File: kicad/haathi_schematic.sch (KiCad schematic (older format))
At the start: 0 parts

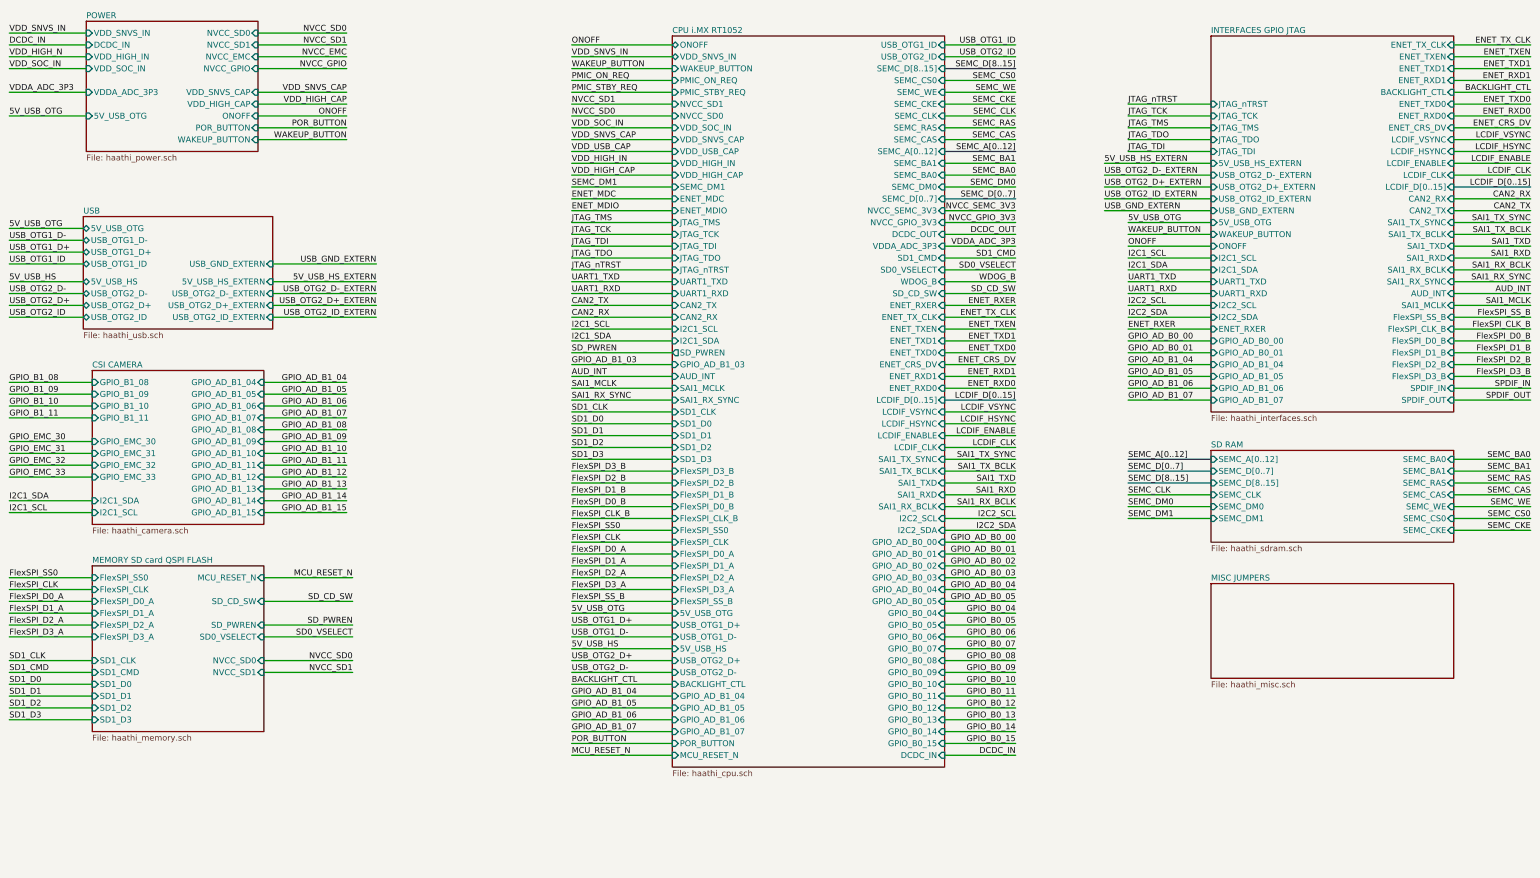
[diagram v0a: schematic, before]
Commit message: Rearrange buttons and LED pin connections
LED pins go to PWM pins
Switches go to previously SPDIF_IN and OUT pins
FlexSPI 2 pins freed up

Signed-off-by: Kumar Abhishek <abhishek@theembeddedkitchen.net>
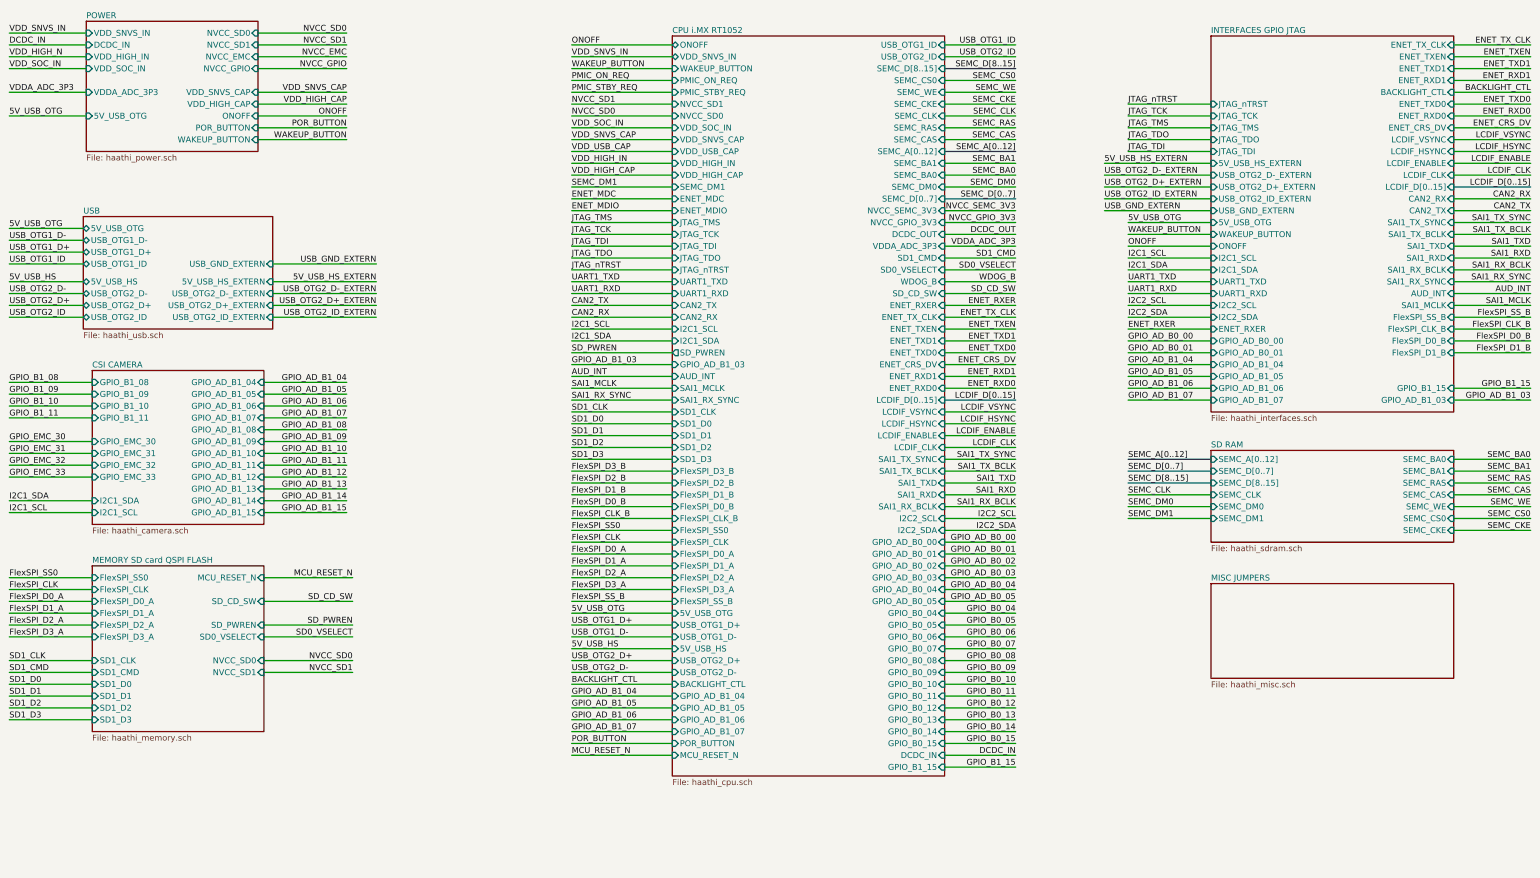
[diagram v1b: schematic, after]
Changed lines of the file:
@@
 EESchema Schematic File Version 4
-LIBS:haathi_schematic-cache
+LIBS:haathi-cache
 EELAYER 26 0
 EELAYER END
 $Descr A3 16535 11693
 encoding utf-8
-Sheet 1 9
+Sheet 3 11
 Title "haathi_cam"
 Date "2018-03-11"
@@
 $EndSheet
 $Sheet
-S 7950 1575 2300 6175
+S 7950 1575 2300 6250
 U 5A6307C3
 F0 "CPU i.MX RT1052" 50
@@
 F122 "USB_OTG1_ID" I R 10250 1650 50
 F123 "USB_OTG2_ID" I R 10250 1750 50
+F124 "GPIO_B1_15" I R 10250 7750 50
 $EndSheet
 $Sheet
@@
 F53 "GPIO_AD_B1_06" I L 12500 4550 50
 F54 "GPIO_AD_B1_07" I L 12500 4650 50
-F55 "FlexSPI_D2_B" I R 14550 4350 50
-F56 "FlexSPI_D3_B" I R 14550 4450 50
-F57 "SPDIF_IN" I R 14550 4550 50
-F58 "SPDIF_OUT" I R 14550 4650 50
+F55 "GPIO_B1_15" I R 14550 4550 50
+F57 "GPIO_AD_B1_03" I R 14550 4650 50
 $EndSheet
 $Sheet
@@
 Wire Wire Line
 	14550 4250 15200 4250
-Wire Wire Line
-	14550 4350 15200 4350
-Wire Wire Line
-	14550 4450 15200 4450
-Wire Wire Line
-	14550 4550 15200 4550
 Wire Wire Line
 	14550 4650 15200 4650
@@
 Text Label 15200 4250 2    50   ~ 0
 FlexSPI_D1_B
-Text Label 15200 4350 2    50   ~ 0
-FlexSPI_D2_B
-Text Label 15200 4450 2    50   ~ 0
-FlexSPI_D3_B
-Text Label 15200 4550 2    50   ~ 0
-SPDIF_IN
 Text Label 15200 4650 2    50   ~ 0
-SPDIF_OUT
+GPIO_AD_B1_03
 Wire Bus Line
 	12500 5150 11800 5150
@@
 Text Label 10850 1750 2    50   ~ 0
 USB_OTG2_ID
+Text Label 15200 4550 2    50   ~ 0
+GPIO_B1_15
+Wire Wire Line
+	10250 7750 10850 7750
+Text Label 10850 7750 2    50   ~ 0
+GPIO_B1_15
+Wire Wire Line
+	14550 4550 15200 4550
 $EndSCHEMATC

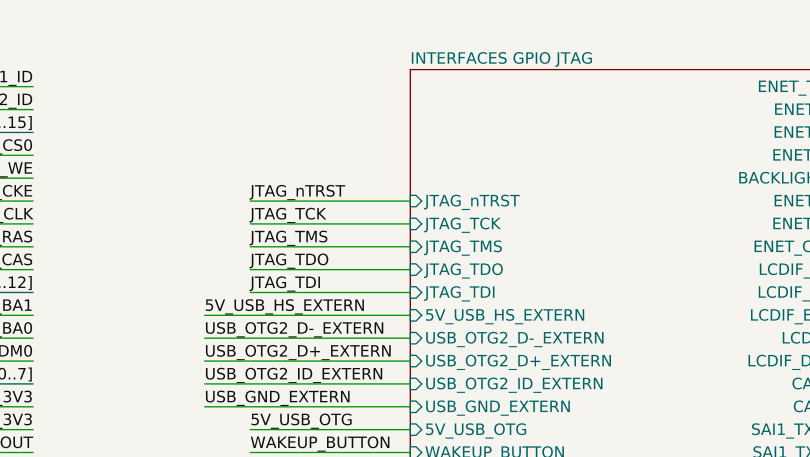
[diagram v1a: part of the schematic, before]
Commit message: Added MCU_RESET_N to interfaces
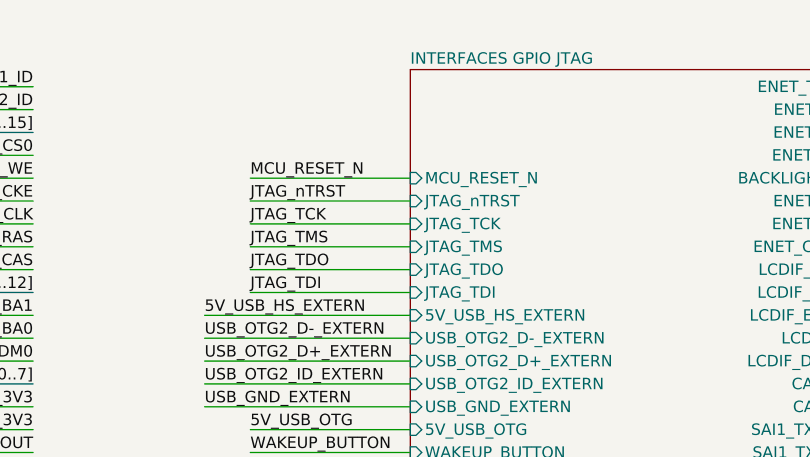
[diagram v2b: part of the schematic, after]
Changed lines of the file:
@@
 EESchema Schematic File Version 4
-LIBS:haathi-cache
+LIBS:haathi_schematic-cache
 EELAYER 26 0
 EELAYER END
 $Descr A3 16535 11693
 encoding utf-8
-Sheet 3 11
+Sheet 1 9
 Title "haathi_cam"
 Date "2018-03-11"
@@
 F54 "GPIO_AD_B1_07" I L 12500 4650 50
 F55 "GPIO_B1_15" I R 14550 4550 50
-F57 "GPIO_AD_B1_03" I R 14550 4650 50
+F56 "GPIO_AD_B1_03" I R 14550 4650 50
+F57 "MCU_RESET_N" I L 12500 2050 50
 $EndSheet
 $Sheet
@@
 Wire Wire Line
 	14550 4550 15200 4550
+Wire Wire Line
+	12500 2050 11800 2050
+Text Label 11800 2050 0    50   ~ 0
+MCU_RESET_N
 $EndSCHEMATC

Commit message: ERC pass 1: Check and resolve the errors
Signed-off-by: Kumar Abhishek <abhishek@theembeddedkitchen.net>
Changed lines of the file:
@@
 EESchema Schematic File Version 4
-LIBS:haathi_schematic-cache
+LIBS:haathi-cache
 EELAYER 26 0
 EELAYER END
 $Descr A3 16535 11693
 encoding utf-8
-Sheet 1 9
+Sheet 3 11
 Title "haathi_cam"
 Date "2018-03-11"
@@
 F52 "GPIO_AD_B1_05" I L 12500 4450 50
 F53 "GPIO_AD_B1_06" I L 12500 4550 50
-F54 "GPIO_AD_B1_07" I L 12500 4650 50
-F55 "GPIO_B1_15" I R 14550 4550 50
-F56 "GPIO_AD_B1_03" I R 14550 4650 50
-F57 "MCU_RESET_N" I L 12500 2050 50
+F54 "GPIO_B1_15" I R 14550 4550 50
+F55 "GPIO_AD_B1_03" I R 14550 4650 50
+F56 "MCU_RESET_N" I L 12500 2050 50
 $EndSheet
 $Sheet
@@
 Wire Wire Line
 	11800 4550 12500 4550
-Wire Wire Line
-	11800 4650 12500 4650
 Text Label 11800 2150 0    50   ~ 0
 JTAG_nTRST
@@
 Text Label 11800 4550 0    50   ~ 0
 GPIO_AD_B1_06
-Text Label 11800 4650 0    50   ~ 0
-GPIO_AD_B1_07
 Text Label 15200 1650 2    50   ~ 0
 ENET_TX_CLK
@@
 DCDC_IN
 Text Label 2350 1750 0    50   ~ 0
-VDD_HIGH_N
+VDD_HIGH_IN
 Text Label 2350 1850 0    50   ~ 0
 VDD_SOC_IN

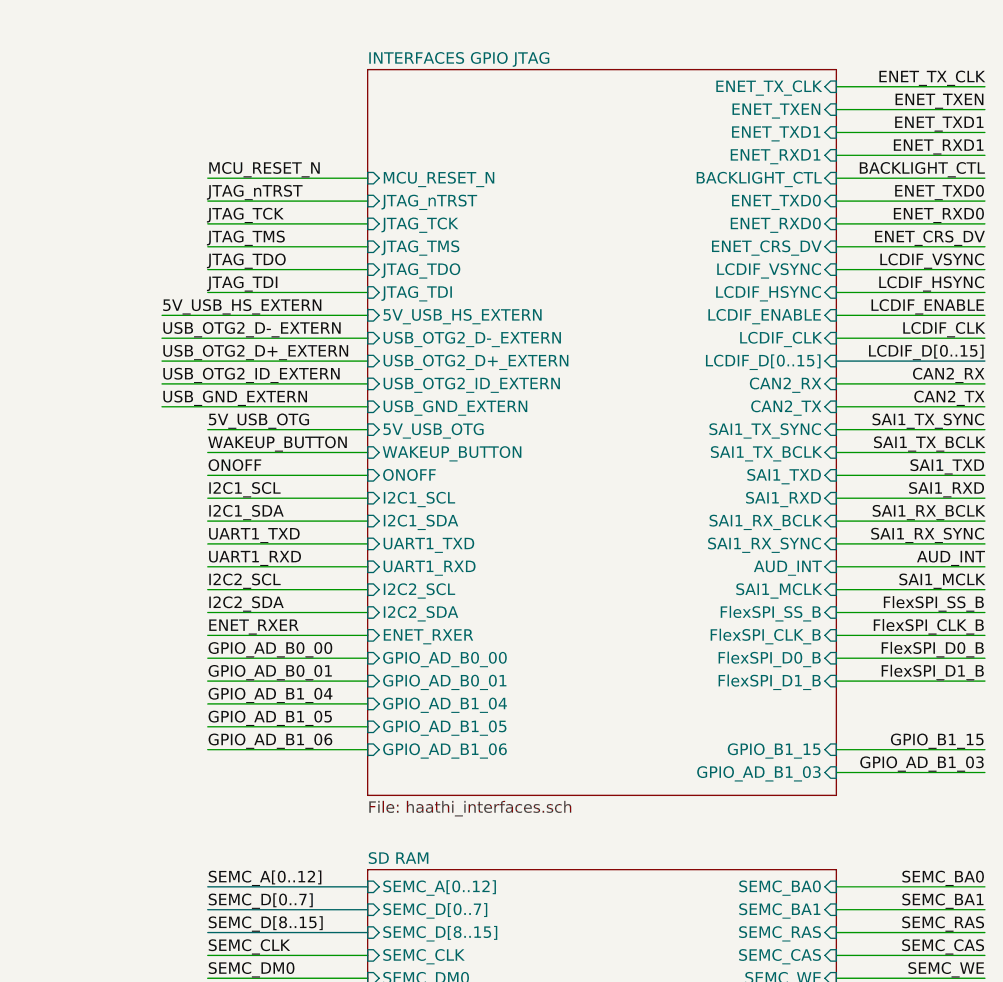
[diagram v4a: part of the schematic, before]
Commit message: Updated interfaces hierarchical labels to top level schematic
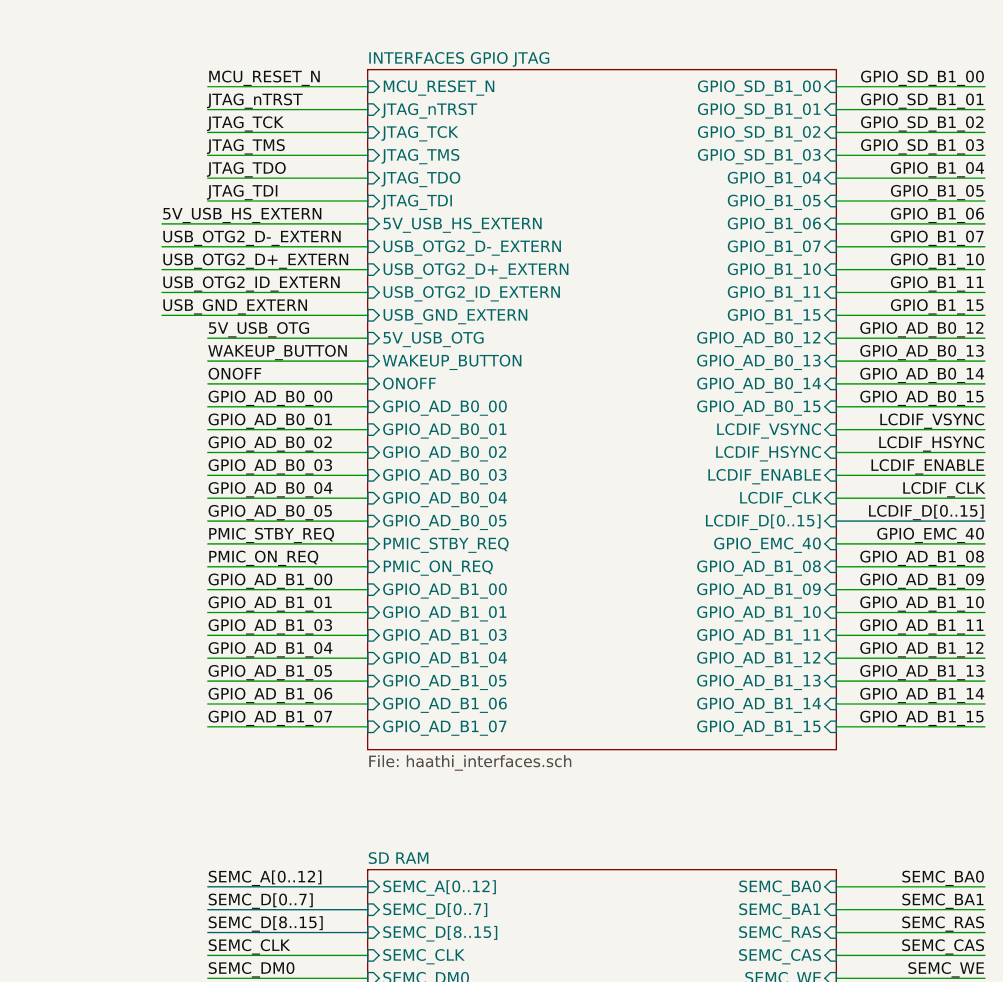
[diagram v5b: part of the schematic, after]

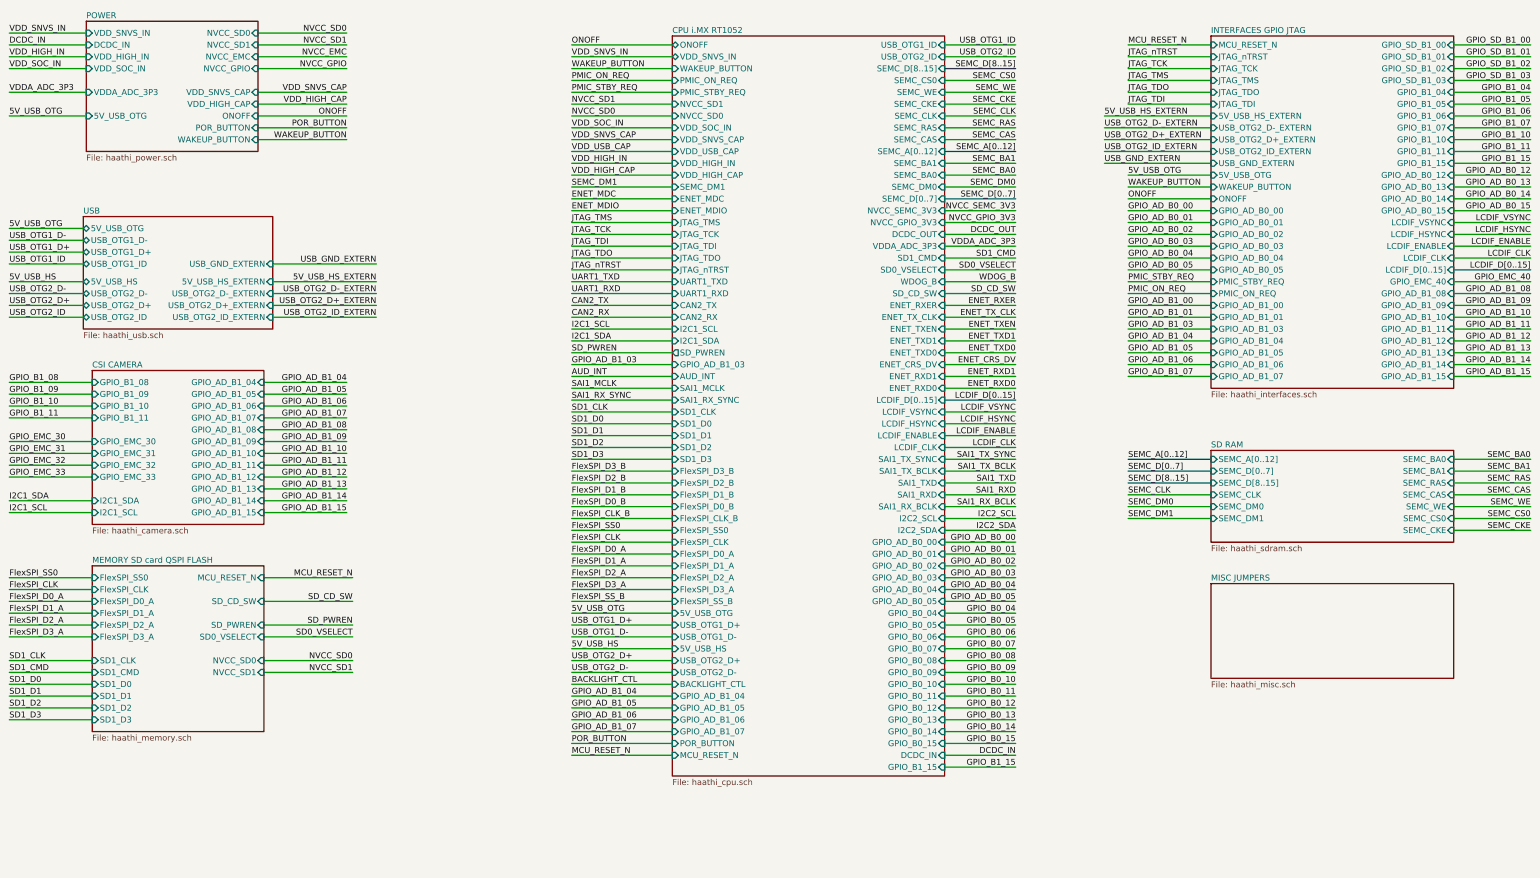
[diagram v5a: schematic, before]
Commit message: Fixes the naming of the hierarchical labels for memory, USB, interfaces and camera sheets
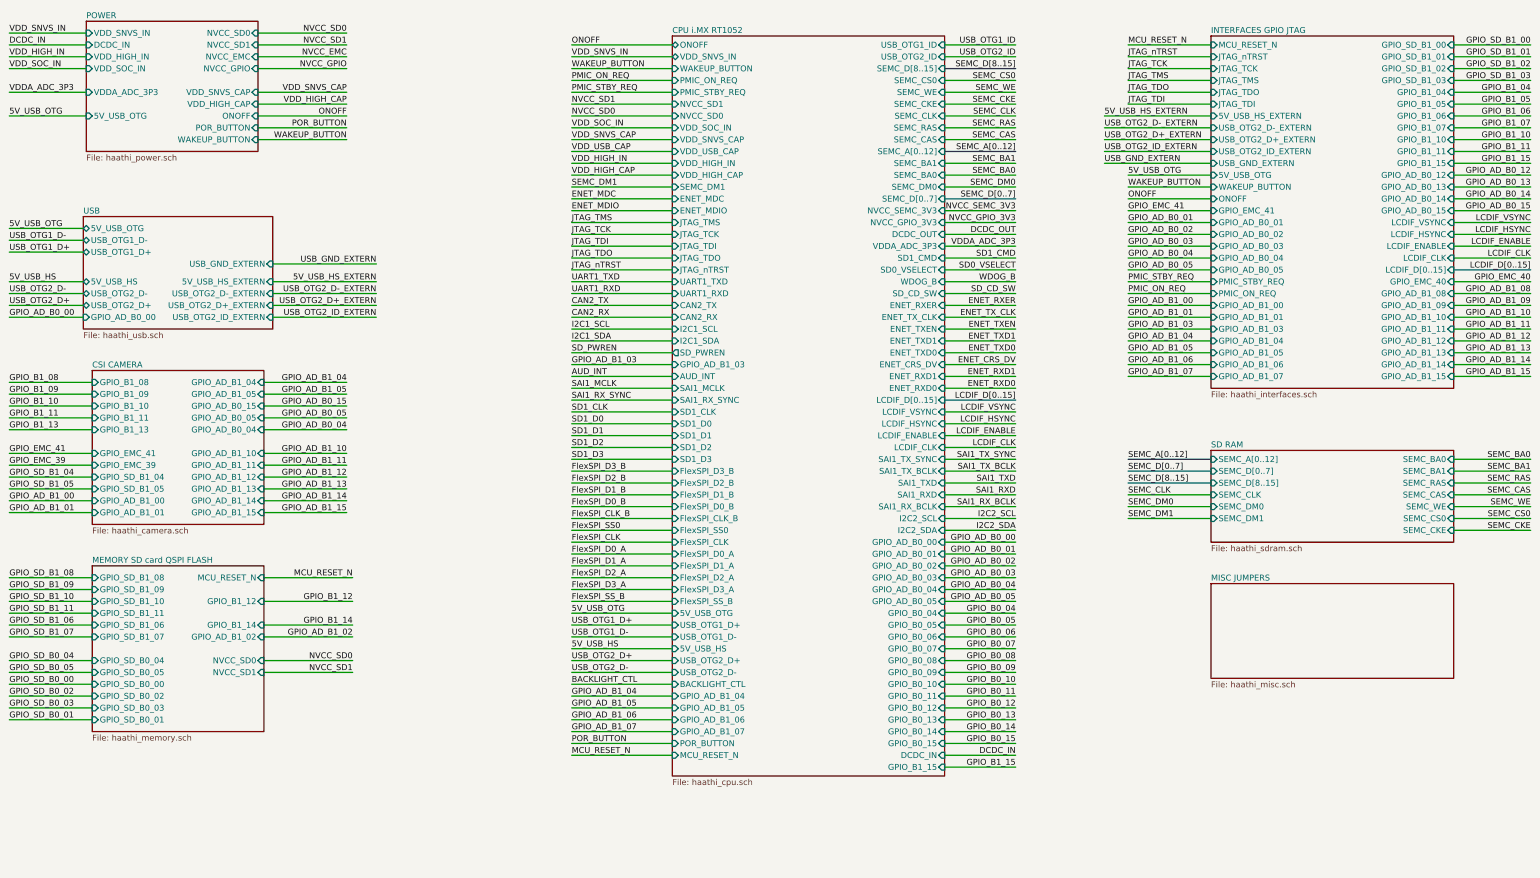
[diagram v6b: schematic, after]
